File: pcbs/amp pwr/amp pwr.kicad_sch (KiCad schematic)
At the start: 38 parts

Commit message: Schematic file fix, misc. PCB
Fixed issue with KiCAD's automatic V5→V6 migration (corrected in 6.0.11) that caused problems with component references in multi-channel schematic sheets
Finished migration in amp ctrl PCB, inc. re-assigning "exclude from BOM" attributes to testpoints, solder jumpers
Added mounting hole to amp ctrl PCB for addl support to Ethernet jacks, power connector through stiffener
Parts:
- C113, C114: renamed from ?; value 10uF 50V X7S -> (none); footprint Capacitor_SMD:C_1210_3225Metric -> (none)
- H1, H10, H11, H12, H13, H14, H15, H16, H17, H18, H2, H21, H24, H29, H3, H32, H4, H5, H6, H7, H8, H9: renamed from ?; value #4/M3 -> (none); footprint MountingHole:MountingHole_3.2mm_M3_DIN965_Pad -> (none)
- J17, J18, J19, J20: renamed from ?; value Conn_02x02_Odd_Even -> (none); footprint Connector_PinHeader_2.54mm:PinHeader_2x02_P2.54mm_Vertical_SMD -> (none)
- R3: renamed from ?; value 0.1 -> (none); footprint Resistor_SMD:R_0805_2012Metric -> (none)
- TP1, TP14, TP38, TP62, TP86: renamed from ?; value TestPoint_Flag -> (none); footprint TestPoint:TestPoint_Keystone_5019_Minature -> (none)
- gave numbers to parts that had none: 4

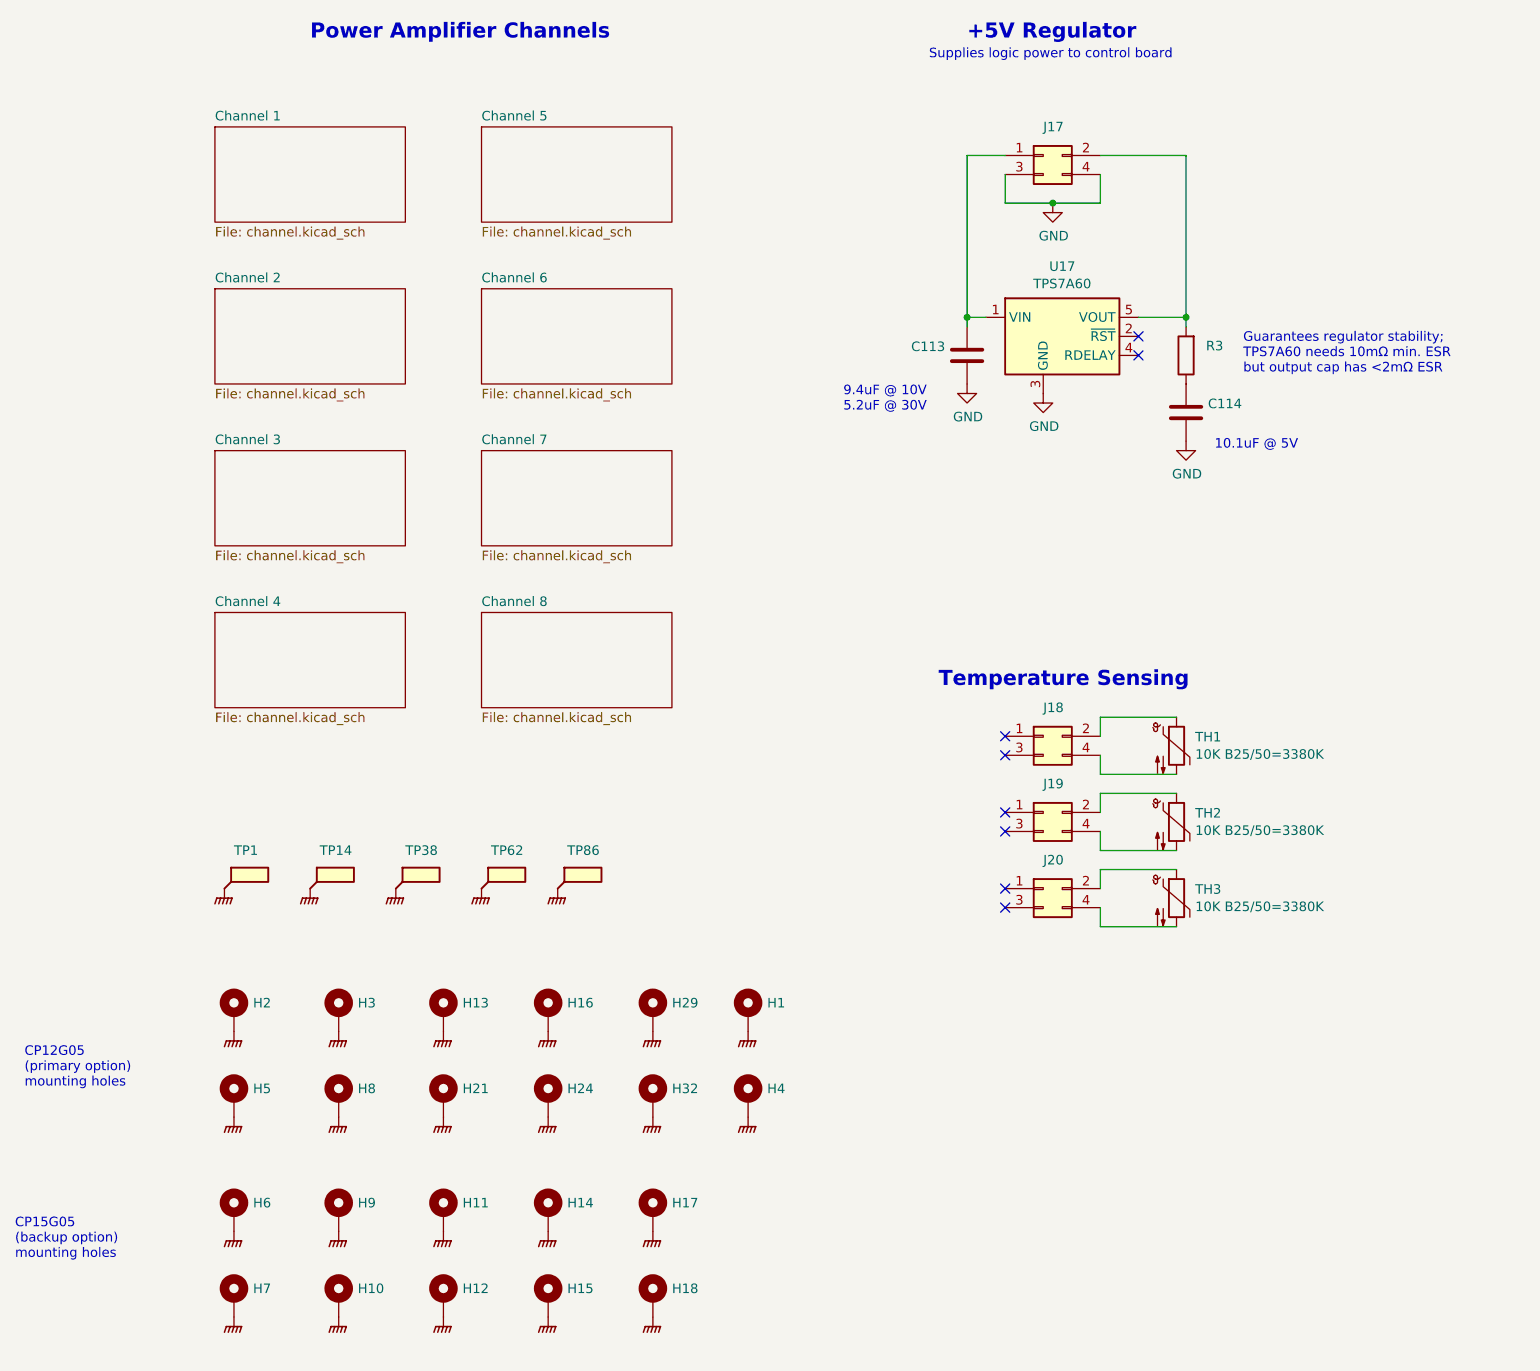
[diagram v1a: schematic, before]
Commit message: Upgraded to KiCAD 7.0 format Added 10µF cap to ADC's REFP pins to fix the voltage reference output (#15) Corrected ADC & DAC reset by adding a separate reset circuit (#14) Increased Cfbk compensation cap on each channel to work out-of-the-box with small coils (#16)
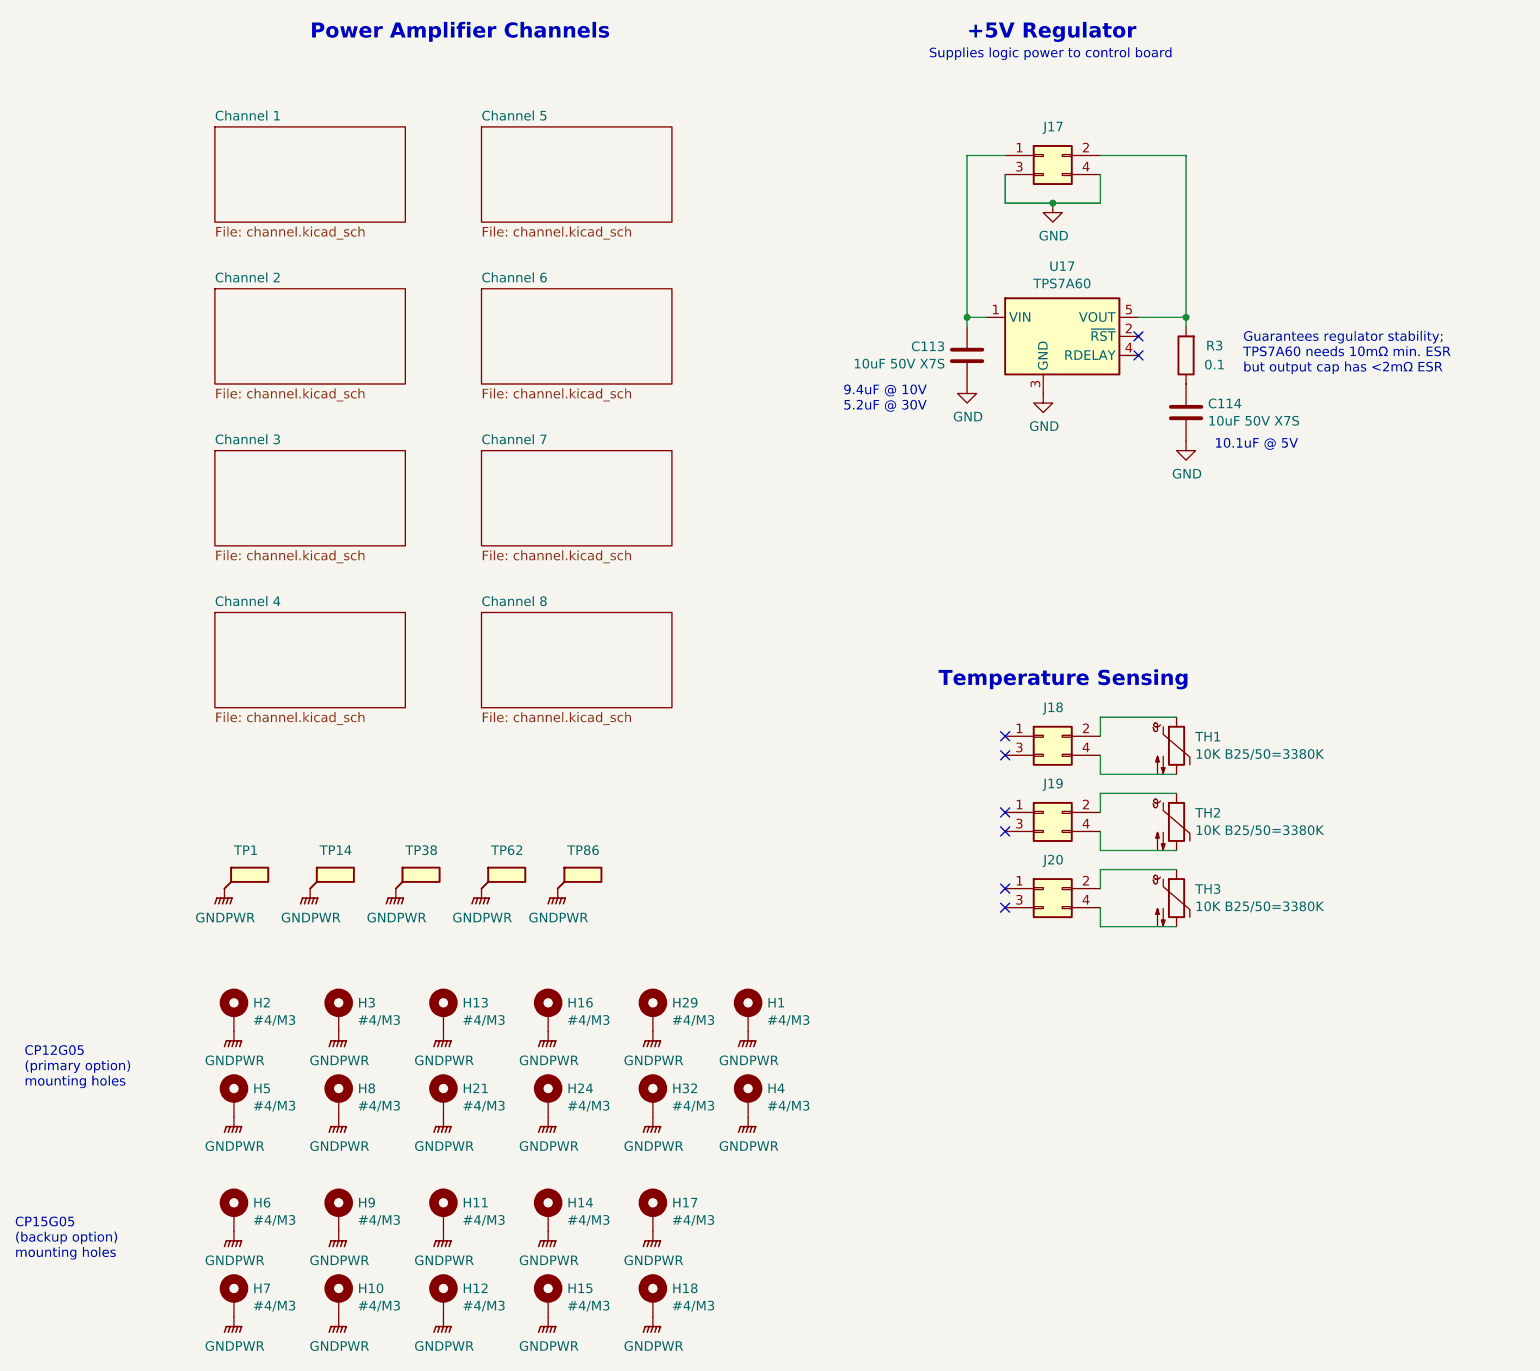
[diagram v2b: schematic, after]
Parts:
- C113, C114: value (none) -> 10uF 50V X7S; footprint (none) -> Capacitor_SMD:C_1210_3225Metric
- H1, H10, H11, H12, H13, H14, H15, H16, H17, H18, H2, H21, H24, H29, H3, H32, H4, H5, H6, H7, H8, H9: value (none) -> #4/M3; footprint (none) -> MountingHole:MountingHole_3.2mm_M3_DIN965_Pad
- J17, J18, J19, J20: value (none) -> Conn_02x02_Odd_Even; footprint (none) -> Connector_PinHeader_2.54mm:PinHeader_2x02_P2.54mm_Vertical_SMD
- R3: value (none) -> 0.1; footprint (none) -> Resistor_SMD:R_0805_2012Metric
- TP1, TP14, TP38, TP62, TP86: value (none) -> TestPoint_Flag; footprint (none) -> TestPoint:TestPoint_Keystone_5019_Minature

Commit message: Finished migrating footprint names
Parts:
- TP1, TP14, TP38, TP62, TP86: footprint TestPoint:TestPoint_Keystone_5019_Minature -> TestPoint:TestPoint_Keystone_5019_Miniature
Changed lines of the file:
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@@
 			)
 		)
-		(property "Footprint" "TestPoint:TestPoint_Keystone_5019_Minature"
+		(property "Footprint" "TestPoint:TestPoint_Keystone_5019_Miniature"
 			(at 46.99 139.7 0)
 			(effects
@@
 			)
 		)
-		(property "Footprint" "TestPoint:TestPoint_Keystone_5019_Minature"
+		(property "Footprint" "TestPoint:TestPoint_Keystone_5019_Miniature"
 			(at 58.42 139.7 0)
 			(effects
@@
 			)
 		)
-		(property "Footprint" "TestPoint:TestPoint_Keystone_5019_Minature"
+		(property "Footprint" "TestPoint:TestPoint_Keystone_5019_Miniature"
 			(at 69.85 139.7 0)
 			(effects
@@
 			)
 		)
-		(property "Footprint" "TestPoint:TestPoint_Keystone_5019_Minature"
+		(property "Footprint" "TestPoint:TestPoint_Keystone_5019_Miniature"
 			(at 81.28 139.7 0)
 			(effects
@@
 			)
 		)
-		(property "Footprint" "TestPoint:TestPoint_Keystone_5019_Minature"
+		(property "Footprint" "TestPoint:TestPoint_Keystone_5019_Miniature"
 			(at 91.44 139.7 0)
 			(effects
